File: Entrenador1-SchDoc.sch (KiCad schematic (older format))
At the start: 87 parts, among them J11 CON8, J3 ICSP, J5 CON8, J6 CON8, J7 CON8, J9 3vias, P1 CONN_01X04, P10 CONN_01X04, P2 CONN_01X04, P3 CONN_01X07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

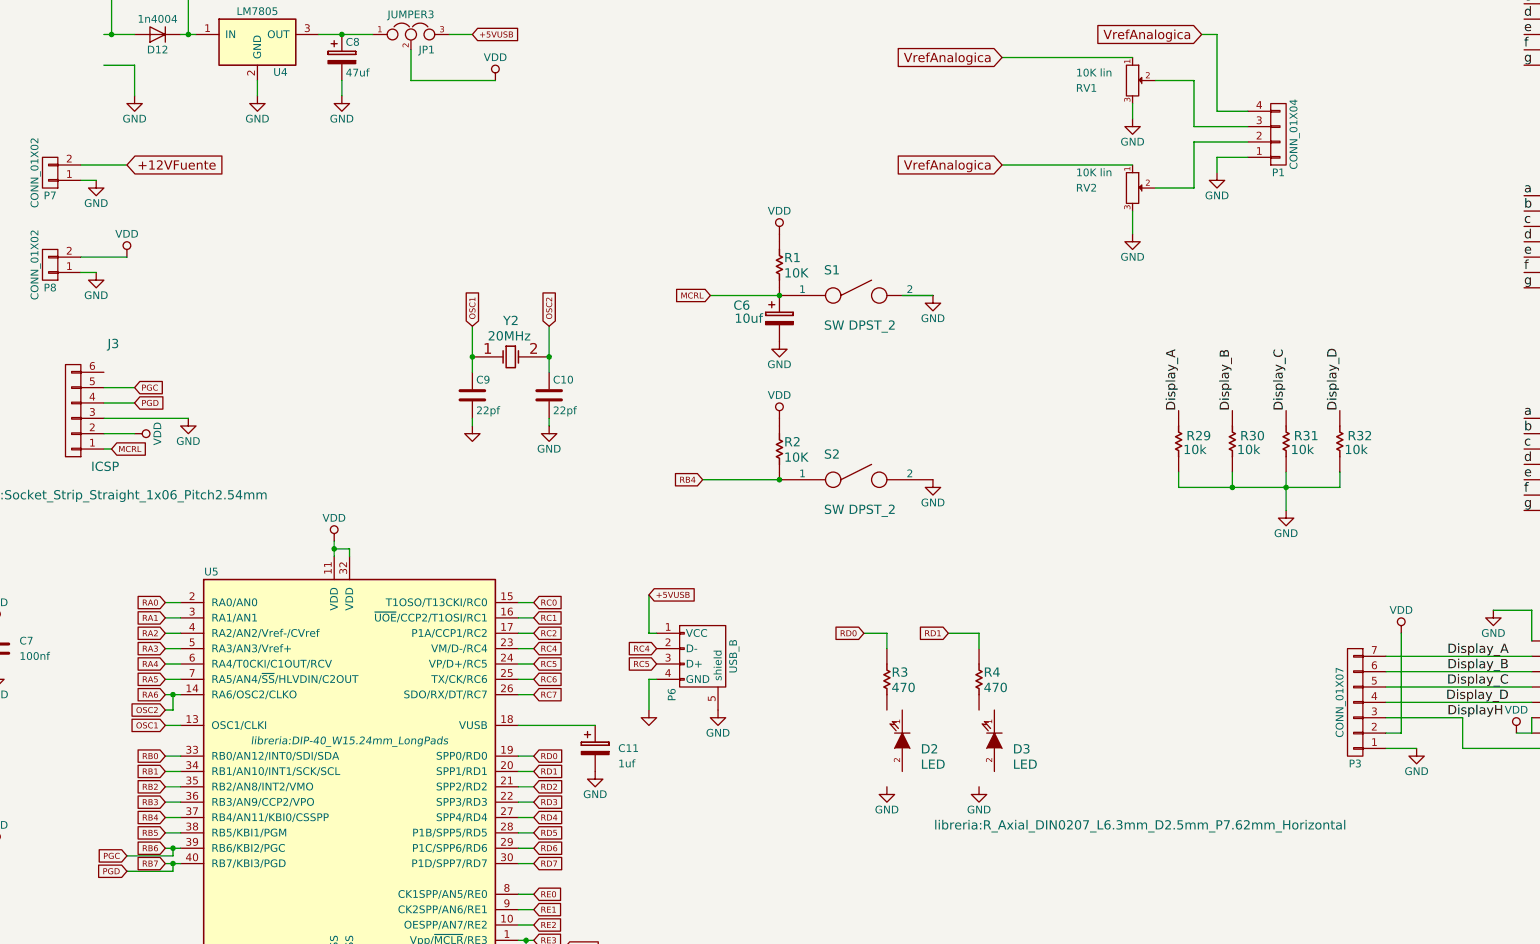
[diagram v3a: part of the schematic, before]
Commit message: Se agrega un diodo de protección a la placa de visualización Se eliminan los pines extra de alimentación de la placa de visualización
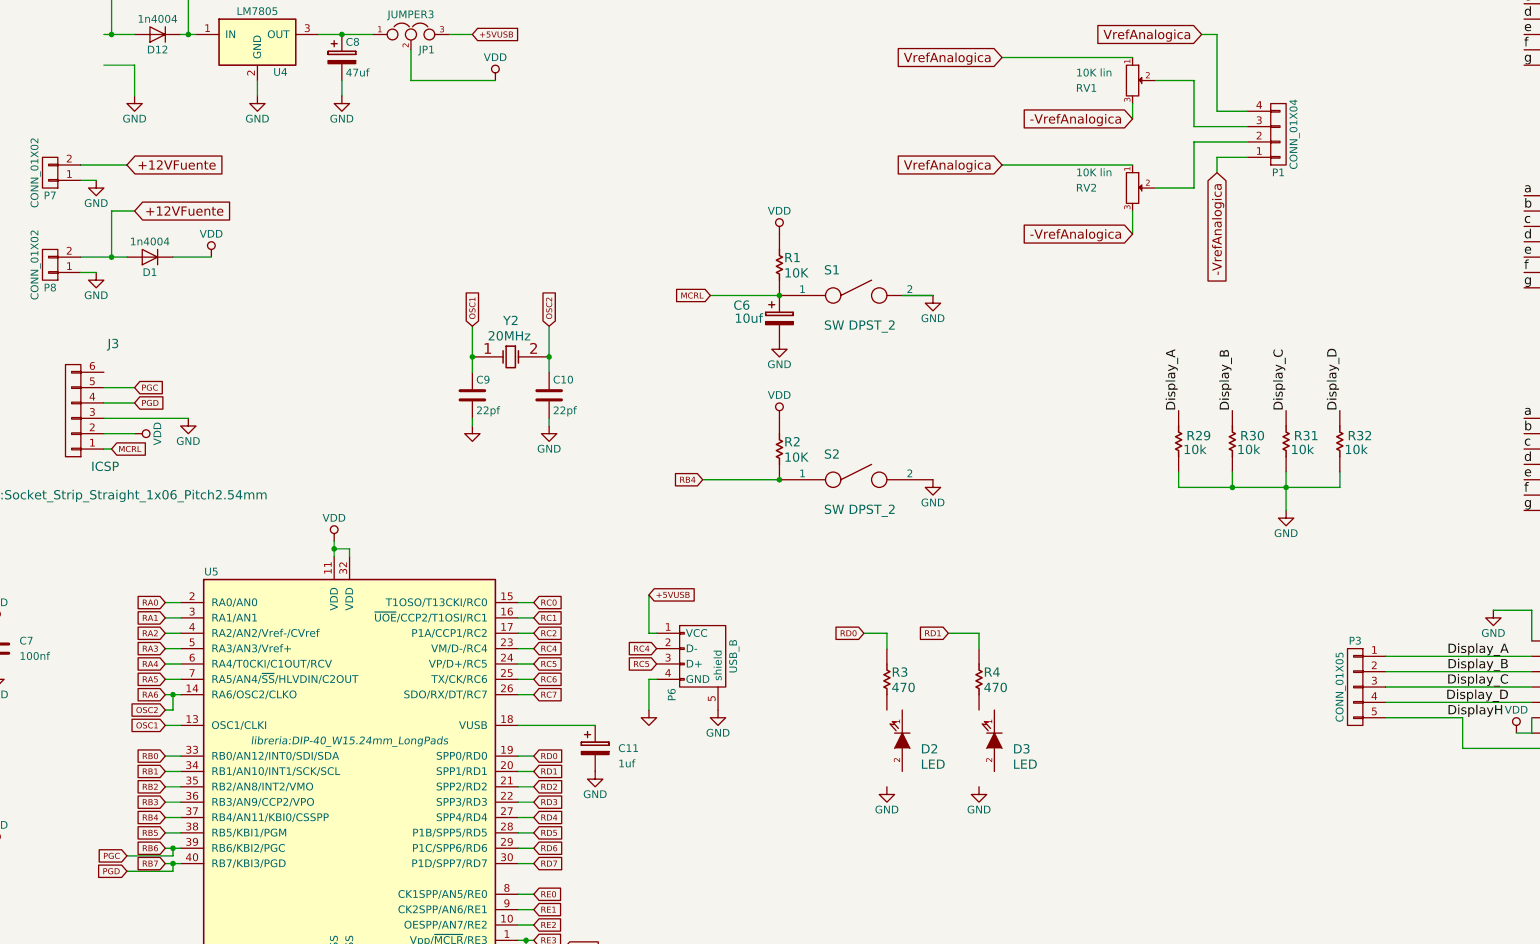
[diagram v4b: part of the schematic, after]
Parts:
- removed P3: CONN_01X07, libreria:Socket_Strip_Straight_1x07_Pitch2.54mm, symbol CONN_01X07
- added D1: 1n4004, libreria:D_5W_P10.16mm_Horizontal, symbol D
- added P3: CONN_01X05, Socket_Strips:Socket_Strip_Straight_1x05_Pitch2.54mm, symbol CONN_01X05
- J7: footprint libreria:Socket_Strip_Straight_1x09_Pitch2.54mm -> libreria:Socket_Strip_Straight_1x08_Pitch2.54mm
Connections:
- net +12VFuente: now also P8.2 (P2), D1.2 (A)
- net DisplayH: now also P3.5 (P5)
- net Display_A: now also P3.1 (P1)
- net Display_B: now also P3.2 (P2)
- net Display_C: now also P3.3 (P3)
- net Display_D: now also P3.4 (P4)
- net GND: no longer P1.1 (P1), RV1.3, RV2.3
- net VDD: now also D1.1 (K); no longer P8.2 (P2)
- new net -VrefAnalogica: P1.1 (P1), RV1.3, RV2.3
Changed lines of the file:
@@
 F 0 "R3" V 9810 8070 60  0000 R TNN
 F 1 "470" V 9710 8070 60  0000 R TNN
-F 2 "libreria:R_Axial_DIN0207_L6.3mm_D2.5mm_P7.62mm_Horizontal" V 8850 6450 60  0000 C CNN
+F 2 "libreria:R_Axial_DIN0207_L6.3mm_D2.5mm_P7.62mm_Horizontal" H 8850 6400 60  0001 C CNN
 F 3 "" H 9710 8070 60  0000 C CNN
 	1    9700 8200
@@
 DisplayH
 $Comp
-L CONN_01X07 P3
-U 1 1 5A54BDF6
-P 12850 8250
-F 0 "P3" H 12850 8650 50  0000 C CNN
-F 1 "CONN_01X07" V 12950 8250 50  0000 C CNN
-F 2 "libreria:Socket_Strip_Straight_1x07_Pitch2.54mm" H 12850 8250 50  0001 C CNN
-F 3 "" H 12850 8250 50  0000 C CNN
-	1    12850 8250
-	-1   0    0    1
-$EndComp
-$Comp
 L CONN_01X04 P1
 U 1 1 5A5A69AC
@@
 Wire Wire Line
 	14550 8600 14550 8500
-Wire Wire Line
-	13250 8550 13050 8550
-Wire Wire Line
-	13150 7800 13150 8450
-Wire Wire Line
-	13150 8450 13050 8450
 Wire Wire Line
 	11800 4200 11800 4500
@@
 F 0 "J7" H 2300 9500 60  0000 L BNN
 F 1 "CON8" H 2300 8500 60  0000 L BNN
-F 2 "libreria:Socket_Strip_Straight_1x09_Pitch2.54mm" H 2400 8350 60  0001 C CNN
+F 2 "libreria:Socket_Strip_Straight_1x08_Pitch2.54mm" H 2400 8350 60  0001 C CNN
 F 3 "" H 2300 8500 60  0000 C CNN
 	1    2400 9100
@@
 $Comp
 L GND #PWR026
-U 1 1 5A66395B
-P 11950 4800
-F 0 "#PWR026" H 11950 4550 50  0001 C CNN
-F 1 "GND" H 11950 4650 50  0000 C CNN
-F 2 "" H 11950 4800 50  0000 C CNN
-F 3 "" H 11950 4800 50  0000 C CNN
-	1    11950 4800
-	1    0    0    -1
-$EndComp
-$Comp
-L GND #PWR027
 U 1 1 5A663BC4
 P 11950 1500
-F 0 "#PWR027" H 11950 1250 50  0001 C CNN
+F 0 "#PWR026" H 11950 1250 50  0001 C CNN
 F 1 "GND" H 11950 1350 50  0000 C CNN
 F 2 "" H 11950 1500 50  0000 C CNN
@@
 $EndComp
 $Comp
-L GND #PWR028
+L GND #PWR027
 U 1 1 5A6650BA
 P 11950 2100
-F 0 "#PWR028" H 11950 1850 50  0001 C CNN
+F 0 "#PWR027" H 11950 1850 50  0001 C CNN
 F 1 "GND" H 11950 1950 50  0000 C CNN
 F 2 "" H 11950 2100 50  0000 C CNN
@@
 $EndComp
 $Comp
-L GND #PWR029
+L GND #PWR028
 U 1 1 5A6655C0
 P 11950 2750
-F 0 "#PWR029" H 11950 2500 50  0001 C CNN
+F 0 "#PWR028" H 11950 2500 50  0001 C CNN
 F 1 "GND" H 11950 2600 50  0000 C CNN
 F 2 "" H 11950 2750 50  0000 C CNN
@@
 $EndComp
 $Comp
-L GND #PWR030
+L GND #PWR029
 U 1 1 5A6656CA
 P 11950 3400
-F 0 "#PWR030" H 11950 3150 50  0001 C CNN
+F 0 "#PWR029" H 11950 3150 50  0001 C CNN
 F 1 "GND" H 11950 3250 50  0000 C CNN
 F 2 "" H 11950 3400 50  0000 C CNN
@@
 	2700 9250 2600 9250
 $Comp
-L GND #PWR031
+L GND #PWR030
 U 1 1 5A6768D2
 P 7100 6450
-F 0 "#PWR031" H 7100 6200 50  0001 C CNN
+F 0 "#PWR030" H 7100 6200 50  0001 C CNN
 F 1 "GND" H 7100 6300 50  0001 C CNN
 F 2 "" H 7100 6450 50  0000 C CNN
@@
 $EndComp
 $Comp
-L GND #PWR032
+L GND #PWR031
 U 1 1 5A6769D9
 P 7600 6450
-F 0 "#PWR032" H 7600 6200 50  0001 C CNN
+F 0 "#PWR031" H 7600 6200 50  0001 C CNN
 F 1 "GND" H 7600 6300 50  0000 C CNN
 F 2 "" H 7600 6450 50  0000 C CNN
@@
 $EndComp
 $Comp
-L GND #PWR033
+L GND #PWR032
 U 1 1 5A676AE0
 P 3850 9300
-F 0 "#PWR033" H 3850 9050 50  0001 C CNN
+F 0 "#PWR032" H 3850 9050 50  0001 C CNN
 F 1 "GND" H 3850 9150 50  0000 C CNN
 F 2 "" H 3850 9300 50  0000 C CNN
@@
 	7100 6400 7100 6450
 $Comp
-L VDD #PWR034
+L VDD #PWR033
 U 1 1 5A679DB8
 P 3750 1150
-F 0 "#PWR034" H 3750 1000 50  0001 C CNN
+F 0 "#PWR033" H 3750 1000 50  0001 C CNN
 F 1 "VDD" H 3750 1300 50  0000 C CNN
 F 2 "" H 3750 1150 50  0000 C CNN
@@
 	3750 1150 3750 1250
 $Comp
-L GND #PWR035
+L GND #PWR034
 U 1 1 5A67ABD8
 P 3750 2250
-F 0 "#PWR035" H 3750 2000 50  0001 C CNN
+F 0 "#PWR034" H 3750 2000 50  0001 C CNN
 F 1 "GND" H 3750 2100 50  0000 C CNN
 F 2 "" H 3750 2250 50  0000 C CNN
@@
 $EndComp
 $Comp
-L VDD #PWR036
-U 1 1 5A67D64A
-P 13150 7800
-F 0 "#PWR036" H 13150 7650 50  0001 C CNN
-F 1 "VDD" H 13150 7950 50  0000 C CNN
-F 2 "" H 13150 7800 50  0000 C CNN
-F 3 "" H 13150 7800 50  0000 C CNN
-	1    13150 7800
-	1    0    0    -1
-$EndComp
-$Comp
-L VDD #PWR037
+L VDD #PWR035
 U 1 1 5A67E56D
 P 13900 8450
-F 0 "#PWR037" H 13900 8300 50  0001 C CNN
+F 0 "#PWR035" H 13900 8300 50  0001 C CNN
 F 1 "VDD" H 13900 8600 50  0000 C CNN
 F 2 "" H 13900 8450 50  0000 C CNN
@@
 $EndComp
 $Comp
-L GND #PWR038
-U 1 1 5A67F43F
-P 13250 8550
-F 0 "#PWR038" H 13250 8300 50  0001 C CNN
-F 1 "GND" H 13250 8400 50  0000 C CNN
-F 2 "" H 13250 8550 50  0000 C CNN
-F 3 "" H 13250 8550 50  0000 C CNN
-	1    13250 8550
-	1    0    0    -1
-$EndComp
-$Comp
-L GND #PWR039
+L GND #PWR036
 U 1 1 5A67FC7E
 P 14550 8600
-F 0 "#PWR039" H 14550 8350 50  0001 C CNN
+F 0 "#PWR036" H 14550 8350 50  0001 C CNN
 F 1 "GND" H 14550 8450 50  0000 C CNN
 F 2 "" H 14550 8600 50  0000 C CNN
@@
 $EndComp
 $Comp
-L GND #PWR040
+L GND #PWR037
 U 1 1 5A67FD85
 P 13750 7650
-F 0 "#PWR040" H 13750 7400 50  0001 C CNN
+F 0 "#PWR037" H 13750 7400 50  0001 C CNN
 F 1 "GND" H 13750 7500 50  0000 C CNN
 F 2 "" H 13750 7650 50  0000 C CNN
@@
 $EndComp
 $Comp
-L GND #PWR041
+L GND #PWR038
 U 1 1 5A68187D
 P 12400 7000
-F 0 "#PWR041" H 12400 6750 50  0001 C CNN
+F 0 "#PWR038" H 12400 6750 50  0001 C CNN
 F 1 "GND" H 12400 6850 50  0000 C CNN
 F 2 "" H 12400 7000 50  0000 C CNN
@@
 $EndComp
 $Comp
-L GND #PWR042
+L GND #PWR039
 U 1 1 5A681984
 P 15550 6900
-F 0 "#PWR042" H 15550 6650 50  0001 C CNN
+F 0 "#PWR039" H 15550 6650 50  0001 C CNN
 F 1 "GND" H 15550 6750 50  0000 C CNN
 F 2 "" H 15550 6900 50  0000 C CNN
@@
 $EndComp
 $Comp
-L GND #PWR043
+L GND #PWR040
 U 1 1 5A681D2B
 P 15500 2550
-F 0 "#PWR043" H 15500 2300 50  0001 C CNN
+F 0 "#PWR040" H 15500 2300 50  0001 C CNN
 F 1 "GND" H 15500 2400 50  0000 C CNN
 F 2 "" H 15500 2550 50  0000 C CNN
@@
 $EndComp
 $Comp
-L GND #PWR044
+L GND #PWR041
 U 1 1 5A682AFE
 P 15550 4000
-F 0 "#PWR044" H 15550 3750 50  0001 C CNN
+F 0 "#PWR041" H 15550 3750 50  0001 C CNN
 F 1 "GND" H 15550 3850 50  0000 C CNN
 F 2 "" H 15550 4000 50  0000 C CNN
@@
 $EndComp
 $Comp
-L GND #PWR045
-U 1 1 5A6840B3
-P 11400 5200
-F 0 "#PWR045" H 11400 4950 50  0001 C CNN
-F 1 "GND" H 11400 5050 50  0000 C CNN
-F 2 "" H 11400 5200 50  0000 C CNN
-F 3 "" H 11400 5200 50  0000 C CNN
-	1    11400 5200
-	1    0    0    -1
-$EndComp
-$Comp
-L GND #PWR046
-U 1 1 5A6841BA
-P 11400 4450
-F 0 "#PWR046" H 11400 4200 50  0001 C CNN
-F 1 "GND" H 11400 4300 50  0000 C CNN
-F 2 "" H 11400 4450 50  0000 C CNN
-F 3 "" H 11400 4450 50  0000 C CNN
-	1    11400 4450
-	1    0    0    -1
-$EndComp
-$Comp
-L GND #PWR047
+L GND #PWR042
 U 1 1 5A685C8F
 P 9800 8800
-F 0 "#PWR047" H 9800 8550 50  0001 C CNN
+F 0 "#PWR042" H 9800 8550 50  0001 C CNN
 F 1 "GND" H 9800 8650 50  0000 C CNN
 F 2 "" H 9800 8800 50  0000 C CNN
@@
 $EndComp
 $Comp
-L GND #PWR048
+L GND #PWR043
 U 1 1 5A685D96
 P 10400 8800
-F 0 "#PWR048" H 10400 8550 50  0001 C CNN
+F 0 "#PWR043" H 10400 8550 50  0001 C CNN
 F 1 "GND" H 10400 8650 50  0000 C CNN
 F 2 "" H 10400 8800 50  0000 C CNN
@@
 $EndComp
 $Comp
-L VDD #PWR049
+L VDD #PWR044
 U 1 1 5A68726B
 P 4000 9200
-F 0 "#PWR049" H 4000 9050 50  0001 C CNN
+F 0 "#PWR044" H 4000 9050 50  0001 C CNN
 F 1 "VDD" H 4000 9350 50  0000 C CNN
 F 2 "" H 4000 9200 50  0000 C CNN
@@
 	8650 5600 9100 5600
 $Comp
-L GND #PWR050
+L GND #PWR045
 U 1 1 5A5BEC7D
 P 15550 5450
-F 0 "#PWR050" H 15550 5200 50  0001 C CNN
+F 0 "#PWR045" H 15550 5200 50  0001 C CNN
 F 1 "GND" H 15550 5300 50  0000 C CNN
 F 2 "" H 15550 5450 50  0000 C CNN
@@
 $EndComp
 $Comp
-L GND #PWR051
+L GND #PWR046
 U 1 1 5A6E94EF
 P 4650 4850
-F 0 "#PWR051" H 4650 4600 50  0001 C CNN
+F 0 "#PWR046" H 4650 4600 50  0001 C CNN
 F 1 "GND" H 4650 4700 50  0000 C CNN
 F 2 "" H 4650 4850 50  0000 C CNN
@@
 $EndComp
 $Comp
-L GND #PWR052
+L GND #PWR047
 U 1 1 5A71E024
 P 4650 5450
-F 0 "#PWR052" H 4650 5200 50  0001 C CNN
+F 0 "#PWR047" H 4650 5200 50  0001 C CNN
 F 1 "GND" H 4650 5300 50  0000 C CNN
 F 2 "" H 4650 5450 50  0000 C CNN
@@
 	4550 5350 4850 5350
 $Comp
-L VDD #PWR053
+L VDD #PWR048
 U 1 1 5A721D25
-P 4850 5350
-F 0 "#PWR053" H 4850 5200 50  0001 C CNN
-F 1 "VDD" H 4850 5500 50  0000 C CNN
-F 2 "" H 4850 5350 50  0000 C CNN
-F 3 "" H 4850 5350 50  0000 C CNN
-	1    4850 5350
+P 5400 5350
+F 0 "#PWR048" H 5400 5200 50  0001 C CNN
+F 1 "VDD" H 5400 5500 50  0000 C CNN
+F 2 "" H 5400 5350 50  0000 C CNN
+F 3 "" H 5400 5350 50  0000 C CNN
+	1    5400 5350
 	1    0    0    -1
 $EndComp
@@
 $EndComp
 $Comp
-L VDD #PWR054
+L VDD #PWR049
 U 1 1 5A724122
 P 2700 2550
-F 0 "#PWR054" H 2700 2400 50  0001 C CNN
+F 0 "#PWR049" H 2700 2400 50  0001 C CNN
 F 1 "VDD" H 2700 2700 50  0000 C CNN
 F 2 "" H 2700 2550 50  0000 C CNN
@@
 Connection ~ 2700 2800
 $Comp
-L GND #PWR055
+L GND #PWR050
 U 1 1 5A724E72
 P 3250 3450
-F 0 "#PWR055" H 3250 3200 50  0001 C CNN
+F 0 "#PWR050" H 3250 3200 50  0001 C CNN
 F 1 "GND" H 3250 3300 50  0000 C CNN
 F 2 "" H 3250 3450 50  0000 C CNN
@@
 	2500 3200 2700 3200
 Connection ~ 2700 3200
+$Comp
+L D D1
+U 1 1 5A7F09D1
+P 5000 5350
+F 0 "D1" H 5000 5450 50  0000 C CNN
+F 1 "1n4004" H 5000 5250 50  0000 C CNN
+F 2 "libreria:D_5W_P10.16mm_Horizontal" H 5000 5350 50  0001 C CNN
+F 3 "" H 5000 5350 50  0000 C CNN
+	1    5000 5350
+	-1   0    0    1
+$EndComp
+$Comp
+L CONN_01X05 P3
+U 1 1 5A7F3B85
+P 12850 8150
+F 0 "P3" H 12850 8450 50  0000 C CNN
+F 1 "CONN_01X05" V 12950 8150 50  0000 C CNN
+F 2 "Socket_Strips:Socket_Strip_Straight_1x05_Pitch2.54mm" H 12850 8150 50  0001 C CNN
+F 3 "" H 12850 8150 50  0000 C CNN
+	1    12850 8150
+	-1   0    0    -1
+$EndComp
+Text GLabel 11950 4800 3    60   Input ~ 0
+-VrefAnalogica
+Text GLabel 11400 5200 0    60   Input ~ 0
+-VrefAnalogica
+Text GLabel 11400 4450 0    60   Input ~ 0
+-VrefAnalogica
+Text GLabel 4900 5050 2    60   Input ~ 0
++12VFuente
+Wire Wire Line
+	4900 5050 4750 5050
+Wire Wire Line
+	4750 5050 4750 5350
+Connection ~ 4750 5350
+Wire Wire Line
+	5400 5350 5150 5350
 $EndSCHEMATC
